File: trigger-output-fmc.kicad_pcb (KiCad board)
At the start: 8 copper layers, 84 x 69 mm, 341 parts, among them J1 MMCX, J10 MMCX, J11 MMCX, J12 MMCX, J13 MMCX, J14 MMCX, J15 MMCX, J16 MMCX, J19 WP Jumper, J2 MMCX, J3 MMCX, J4 MMCX, J5 MMCX, J6 MMCX, J7 MMCX, J8 MMCX, J9 MMCX, P1 ASP-134488-01, Q1 FDN335N, Q2 FDN335N, Q3 FDN335N, T1 TCM2-43X+, T2 TCM2-43X+, T3 TCM2-43X+, T4 TCM2-43X+, U1 TLV3601, U10 SN74LVC2G126, U11 TLV3601, U12 SN74LVC2G126, U13 TLV3601, U14 SN74LVC2G126, U15 TLV3601, U16 SN74LVC2G126, U17 TLV3601, U18 SI5394, U19 SI5394, U2 TLV3601, U20 TLV75733PDBV, U21 TLV75718PDBV, U22 TPS563200, U23 74AVC4T245, U24 TLV75733PDBV, U25 74AVC4T245, U26 74LVC8T245, U27 74LVC8T245, U28 TLV75718PDBV, U29 SN74LVC2G126, U3 TLV3601, U30 TLV3601, U31 SN74LVC2G126, U32 TLV3601, U33 SN74LVC2G126, U34 TLV3601, U35 SN74LVC2G126, U36 TLV3601, U37 SN74LVC2G126, U38 TLV3601, U39 SN74LVC2G126, U4 SN74LVC2G126, U40 TLV3601, U41 SN74LVC2G126, U42 TLV3601, U43 SN74LVC2G126, U44 LP3855EMP-ADJ/NOPB, U48 SN74LVC2G126, U5 SN74LVC2G126, U6 TLV3601, U7 SN74LVC2G126, U8 TLV3601, U9 AT24C64D, Y1 CX3225SB48000D0FPJC1, Y2 CX3225SB48000D0FPJC1

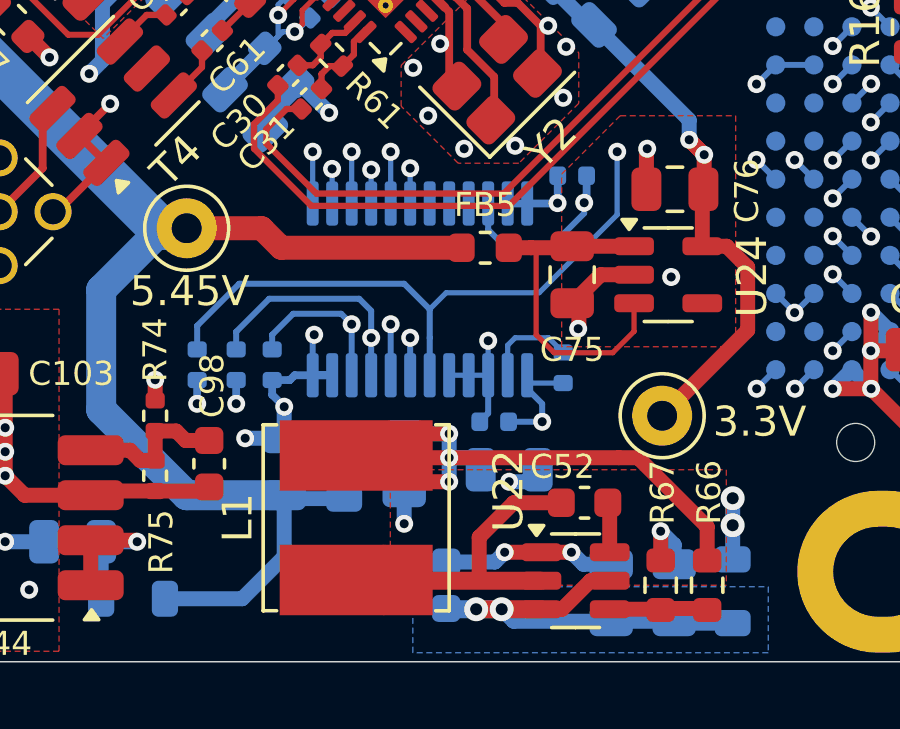
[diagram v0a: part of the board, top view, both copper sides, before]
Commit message: Added 50mA load with LED
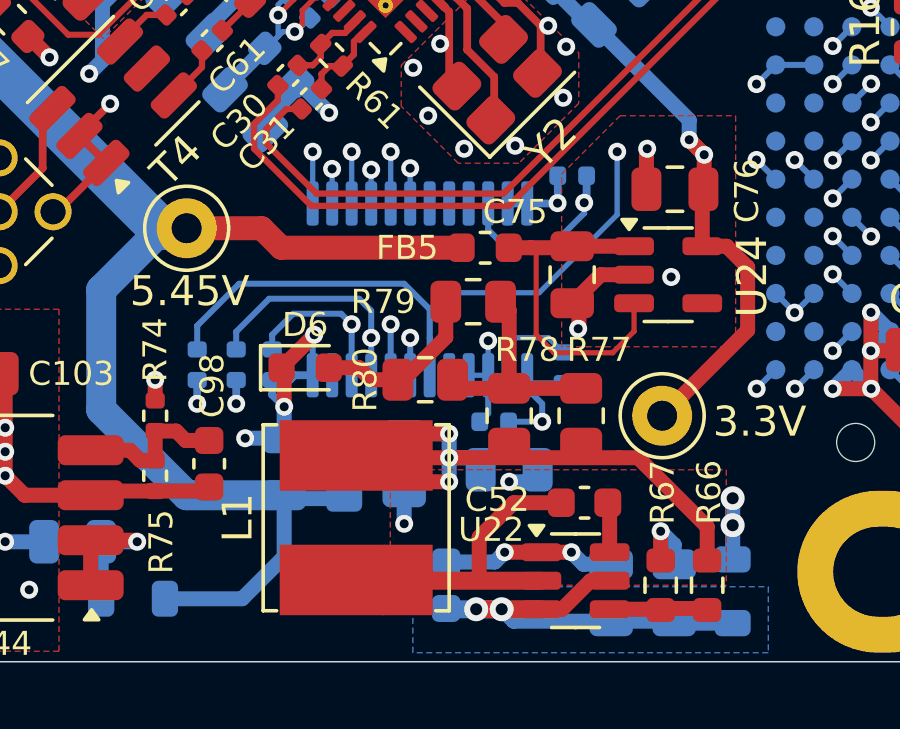
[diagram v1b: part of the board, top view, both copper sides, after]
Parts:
- added D6: Green, LED_SMD:LED_0603_1608Metric, F.Cu at (153.2, 130.2)
- added R77: 88.7R, Resistor_SMD:R_0805_2012Metric, F.Cu at (162.4, 131.8)
- added R78: 88.7R, Resistor_SMD:R_0805_2012Metric, F.Cu at (160.0, 131.8)
- added R79: 88.7R, Resistor_SMD:R_0805_2012Metric, F.Cu at (158.8, 128.0)
- added R80: 88.7R, Resistor_SMD:R_0805_2012Metric, F.Cu at (157.2, 130.6)
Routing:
- net Net-(R77-Pad1): track 0.00 -> 7.41 mm
- net Net-(D6-A): track 0.00 -> 5.84 mm
- net GND: track 518.6 -> 521.5 mm
